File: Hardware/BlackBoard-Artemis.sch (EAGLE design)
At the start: 84 parts, among them IC3 LM1117, J2 CORTEX_DEBUG, J3 POWER_JACKTOE, J5 USB-C, Q1 1.1A/60V/600mΩ, U1 ARTEMIS_MODULESMD, U3 AP2112-3.3V, U5 CH340C, Y1 32.768kHz

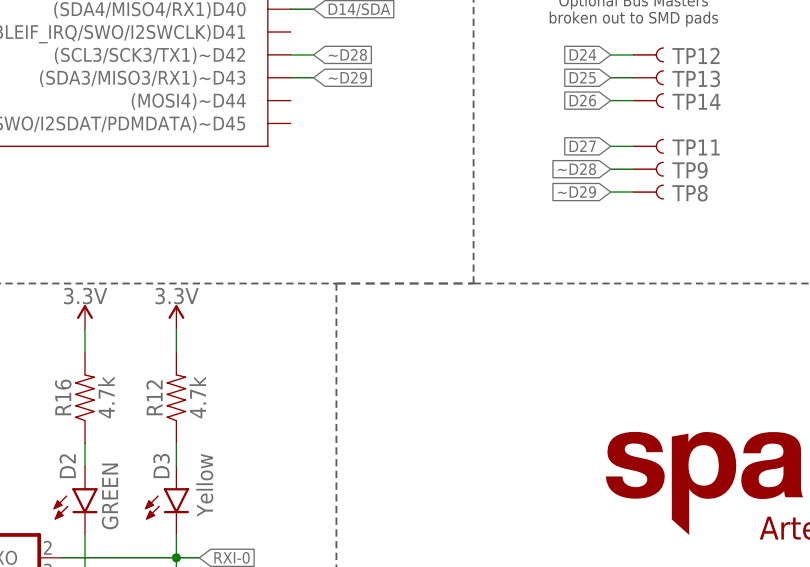
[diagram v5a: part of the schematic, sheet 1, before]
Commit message: Adding ignore. Adding production panel.
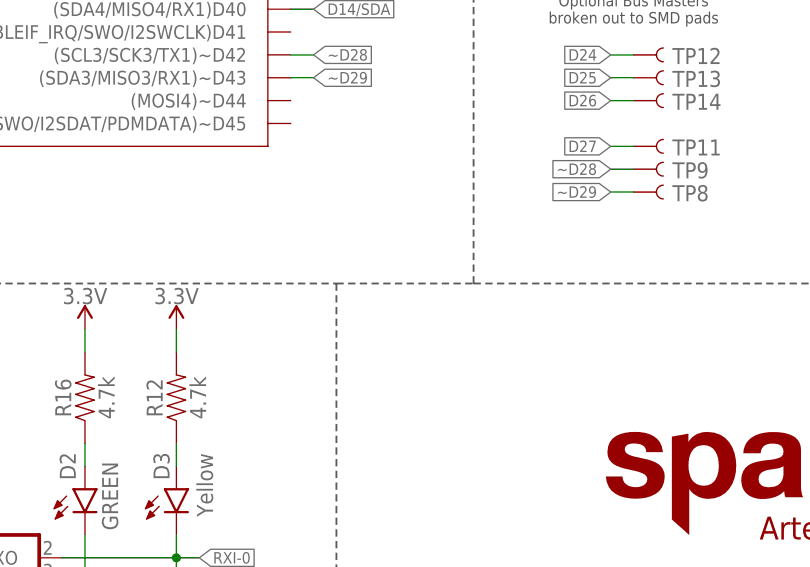
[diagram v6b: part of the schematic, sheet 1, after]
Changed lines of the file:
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@@
 <text x="170.434" y="11.176" size="2.54" layer="94" font="vector">N. Seidle</text>
 <text x="238.76" y="7.62" size="2.54" layer="94" font="vector">X03</text>
-<wire x1="147.32" y1="68.58" x2="162.56" y2="68.58" width="0.254" layer="97" style="longdash"/>
+<wire x1="147.32" y1="68.58" x2="162.56" y2="68.58" width="0.2032" layer="97" style="longdash"/>
 <wire x1="162.56" y1="68.58" x2="248.92" y2="68.58" width="0.2032" layer="97" style="longdash"/>
 <wire x1="147.32" y1="68.58" x2="147.32" y2="0" width="0.2032" layer="97" style="longdash"/>
